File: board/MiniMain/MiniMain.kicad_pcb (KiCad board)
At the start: 2 copper layers, 50.8 x 22.9 mm, 42 parts, among them IC1 ESP32-S2-MINI-1-N4R2, J1 USB4105-GF-A, J10 Conn_01x03_Male, J2 Conn_01x04, J3 Conn_01x16, J5 Conn_01x12, J8 Conn_01x02, Q1 DMP3130LQ-7, SW1 SW_Push, SW2 SW_Push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

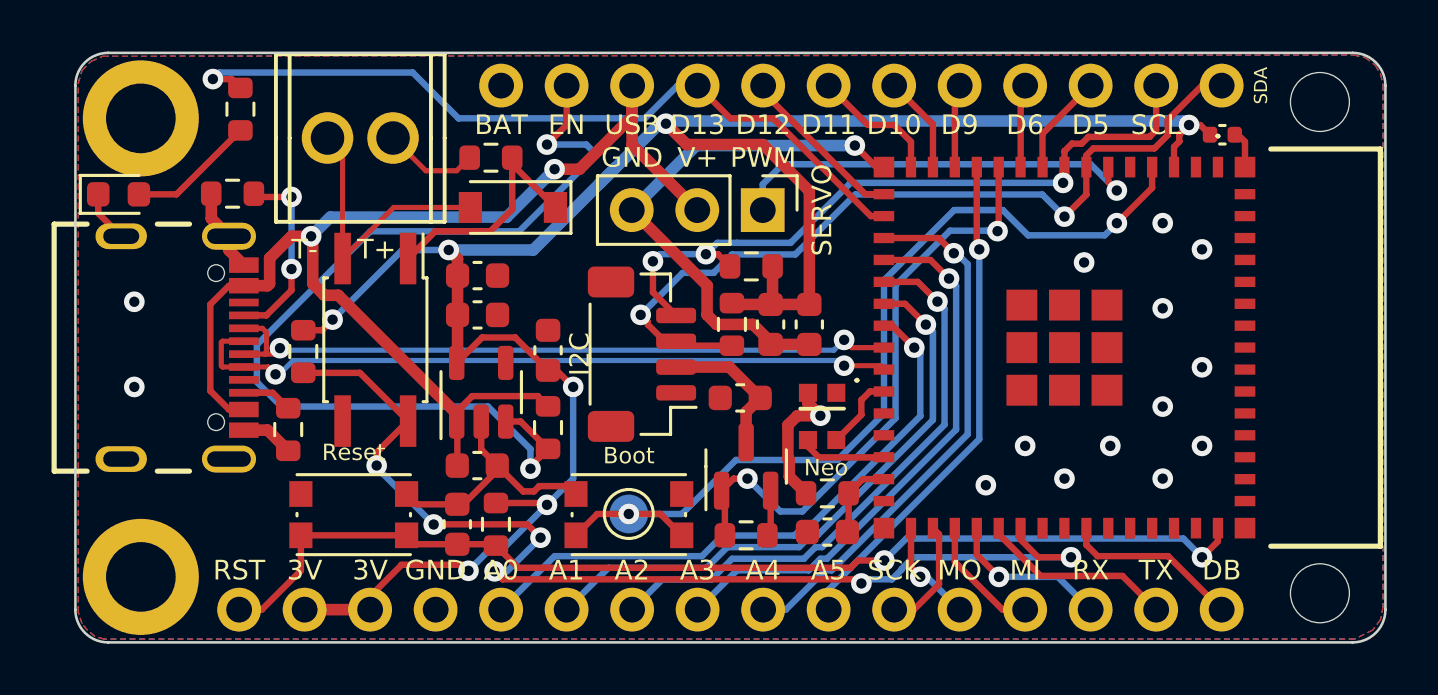
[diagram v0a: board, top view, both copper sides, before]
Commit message: Fix a few unconnected nets. DRC now shows nothing unconnected.
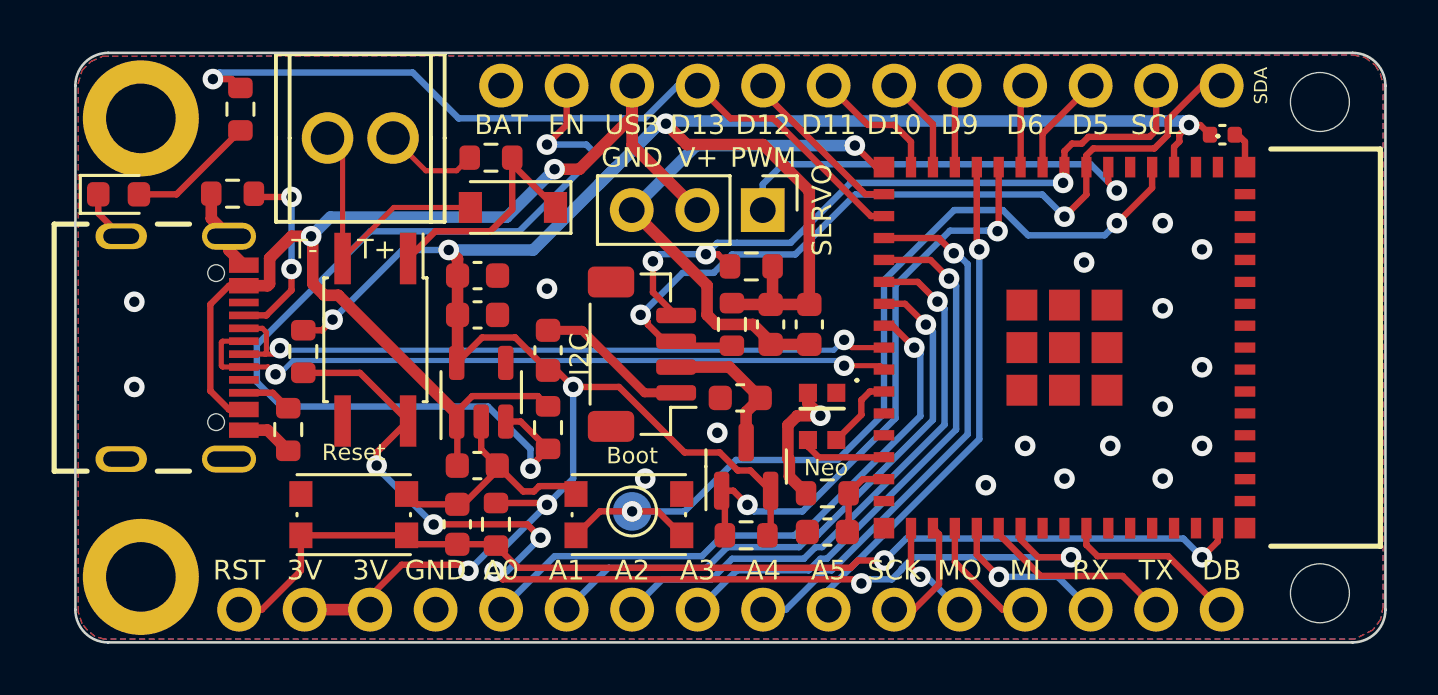
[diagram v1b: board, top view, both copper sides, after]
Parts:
- moved TP1 0.16 mm to (125.7, 101.6)
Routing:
- net +3V3: track 87.8 -> 97.2 mm
- net GND: track 45.3 -> 51.3 mm, vias 16 -> 19
